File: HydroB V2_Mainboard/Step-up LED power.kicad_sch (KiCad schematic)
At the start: 18 parts, among them Q1 S8050

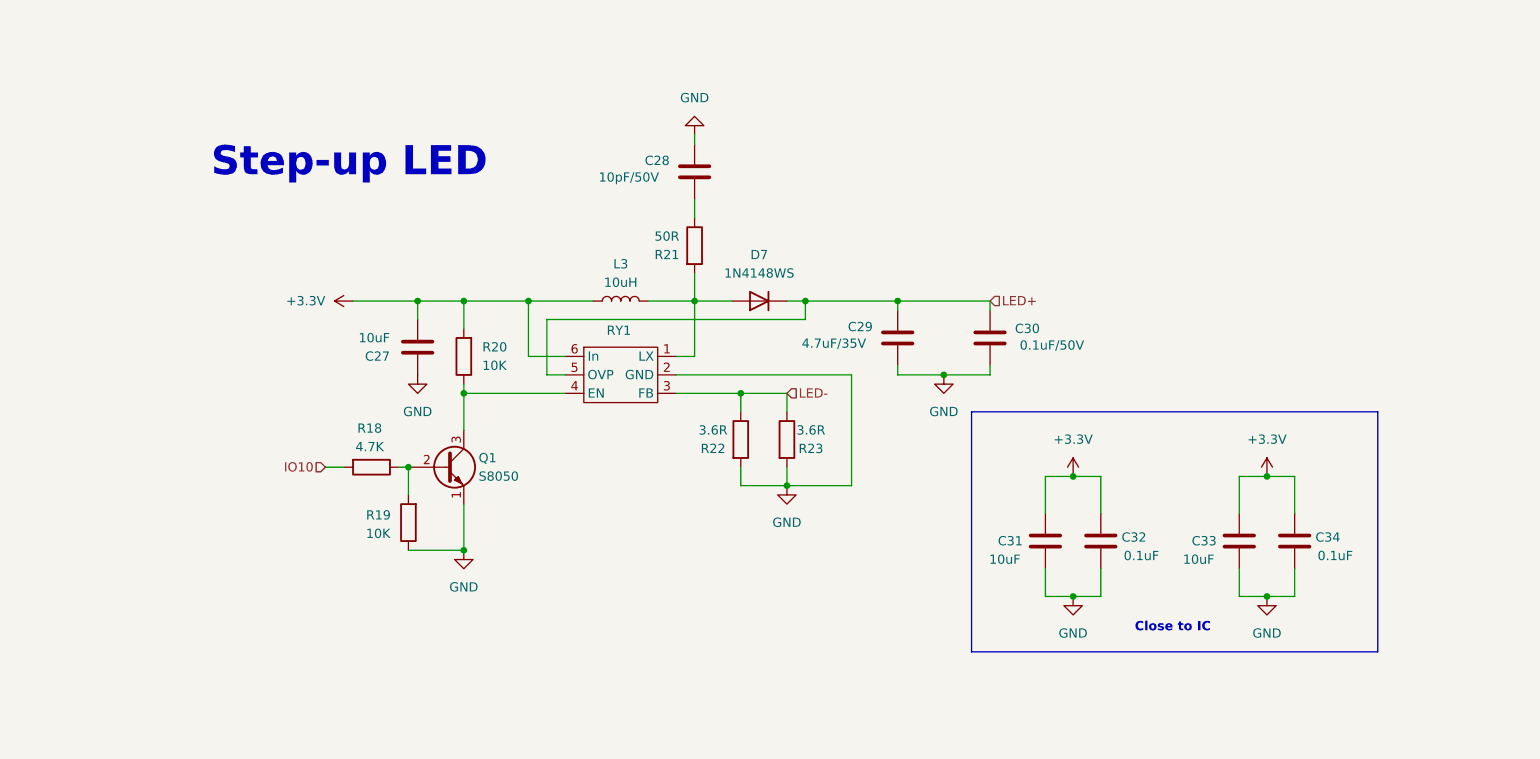
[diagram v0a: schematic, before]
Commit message: Update LCD schematic
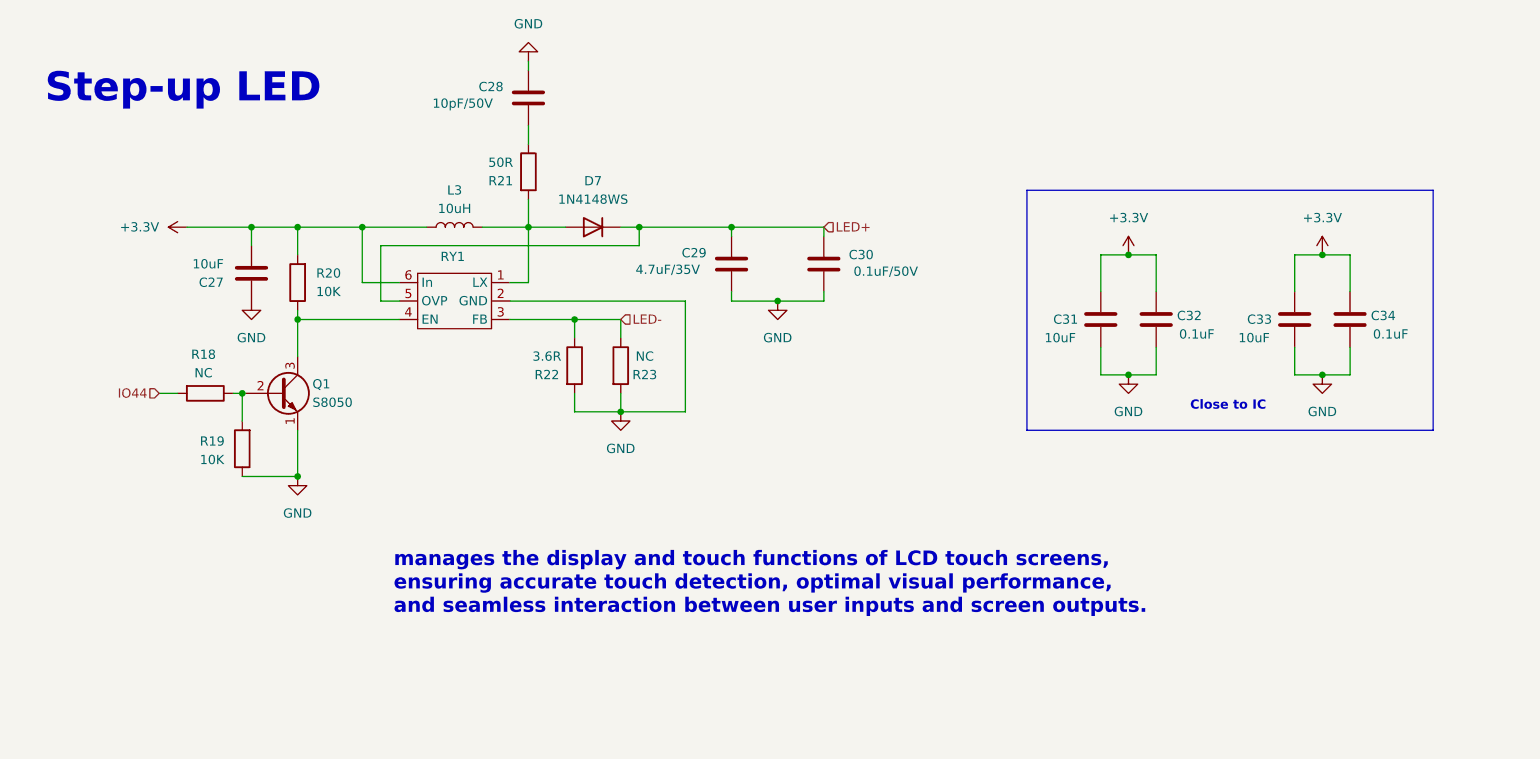
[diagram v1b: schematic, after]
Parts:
- R18: value 4.7K -> NC
- R23: value 3.6R -> NC
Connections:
- net IO10 renamed IO44
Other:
- note added: "manages the display and touch functions of LCD touch screens, ensuring accurate touch detection, optimal visual performance, and seamless interaction between user inputs and screen outputs."
- moved on the sheet: C27, C28, C29, C30, C31, C32, C33, C34, D7, L3, Q1, R18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

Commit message: mainboard updated
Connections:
- net IO44 renamed IO35
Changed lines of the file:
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@@
 		)
 	)
-	(hierarchical_label "IO44"
+	(hierarchical_label "IO35"
 		(shape input)
 		(at 55.88 99.06 180)

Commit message: Schematic mainboard update
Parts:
- removed Q1: S8050, Package_TO_SOT_THT:TO-92_Inline, symbol Transistor_BJT:S8050
- removed R18: NC, Resistor_SMD:R_0603_1608Metric, symbol Device:R
- removed R19: 10K, Resistor_SMD:R_0603_1608Metric, symbol Device:R
- added C13: 1nF/16V, Capacitor_SMD:C_0805_2012Metric, symbol Device:C
- added C14: 100nF/16V, Capacitor_SMD:C_0603_1608Metric, symbol Device:C
- added R16: 100k, Resistor_SMD:R_0603_1608Metric, symbol Device:R
- added R17: 10R, Resistor_SMD:R_0603_1608Metric, symbol Device:R
- C27: value 10uF -> 100nF/16V
- C28: value 10pF/50V -> 1nF/16V; footprint Capacitor_SMD:C_0805_2012Metric -> Capacitor_SMD:C_0603_1608Metric
- C29: value 4.7uF/35V -> 100nF/16V; footprint Capacitor_Tantalum_SMD:CP_EIA-7343-43_Kemet-X_Pad2.25x2.55mm_HandSolder -> Capacitor_Tantalum_SMD:CP_EIA-6032-28_Kemet-C
- C30: value 0.1uF/50V -> 100nF/16V; footprint Capacitor_Tantalum_SMD:CP_EIA-7343-43_Kemet-X_Pad2.25x2.55mm_HandSolder -> Capacitor_SMD:C_0603_1608Metric
- L3: footprint Inductor_SMD:L_Bourns_SRR1260 -> Inductor_SMD:L_Bourns_SRP5030T
- R20: value 10K -> 1k
- R21: value 50R -> 10R
- R22: value 3.6R -> 2R
- R23: value NC -> 2R
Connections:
- net +3.3V: no longer C27.2, L3.1, R20.2, RY1.6 (In)
- net GND: now also R21.1, C14.1, R16.2; no longer C28.2
- net LED+: now also C13.1, C14.2
- net at R20.1, RY1.4 (EN): now also R16.1
- net at D7.2 (A), L3.2, RY1.1 (SW): now also C28.1, R17.1; no longer R21.2
- new net: C13.2, R17.2
- new net: C28.2, R21.2
- new net +5V: C27.2, L3.1, RY1.6 (IN)
- new net BL_PWM: R20.2
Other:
- note added: "- Manages the display and touch functions of LCD touch screens - Ensuring accurate touch detection, optimal visual performance and seamless interaction between user inputs and screen outputs"
- note removed: "manages the display and touch functions of LCD touch screens, ensuring accurate touch detection, optimal visual performance, and seamless interaction between user inputs and screen outputs."
- moved on the sheet: C27, C28, C29, C30, R21

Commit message: Mainboard schematic update
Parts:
- removed C31: 10uF, Capacitor_SMD:C_0603_1608Metric, symbol Device:C
- removed C32: 0.1uF, Capacitor_SMD:C_0603_1608Metric, symbol Device:C
- C13, C28: value 1nF/16V -> 1nF
- C14, C27: value 100nF/16V -> 100nF
- C29: footprint Capacitor_Tantalum_SMD:CP_EIA-6032-28_Kemet-C -> Capacitor_Tantalum_SMD:CP_EIA-3216-10_Kemet-I
- C30: footprint Capacitor_SMD:C_0603_1608Metric -> Capacitor_Tantalum_SMD:CP_EIA-3216-10_Kemet-I
- C33: value 10uF -> 100nF
- C34: value 0.1uF -> 100nF
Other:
- note added: "- Manages the display and touch functions of LCD touchscreens - Ensuring accurate touch detection, optimal visual performance and seamless interaction between user inputs and screen outputs"
- note removed: "- Manages the display and touch functions of LCD touch screens - Ensuring accurate touch detection, optimal visual performance and seamless interaction between user inputs and screen outputs"
